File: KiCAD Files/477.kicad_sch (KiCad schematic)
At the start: 28 parts, among them IC1 W25N01GVSFIG, IC2 W25N01GVSFIG, IC3 W25N01GVSFIG, IC4 W25N01GVSFIG, IC6 USBLC6-2SC6, J1 BM06B-SRSS-TBT_LF__SN_, J2 6364372-2, J5 BM07B-SRSS-TB_LF__SN_, J6 BM09B-SRSS-TB_LF__SN_

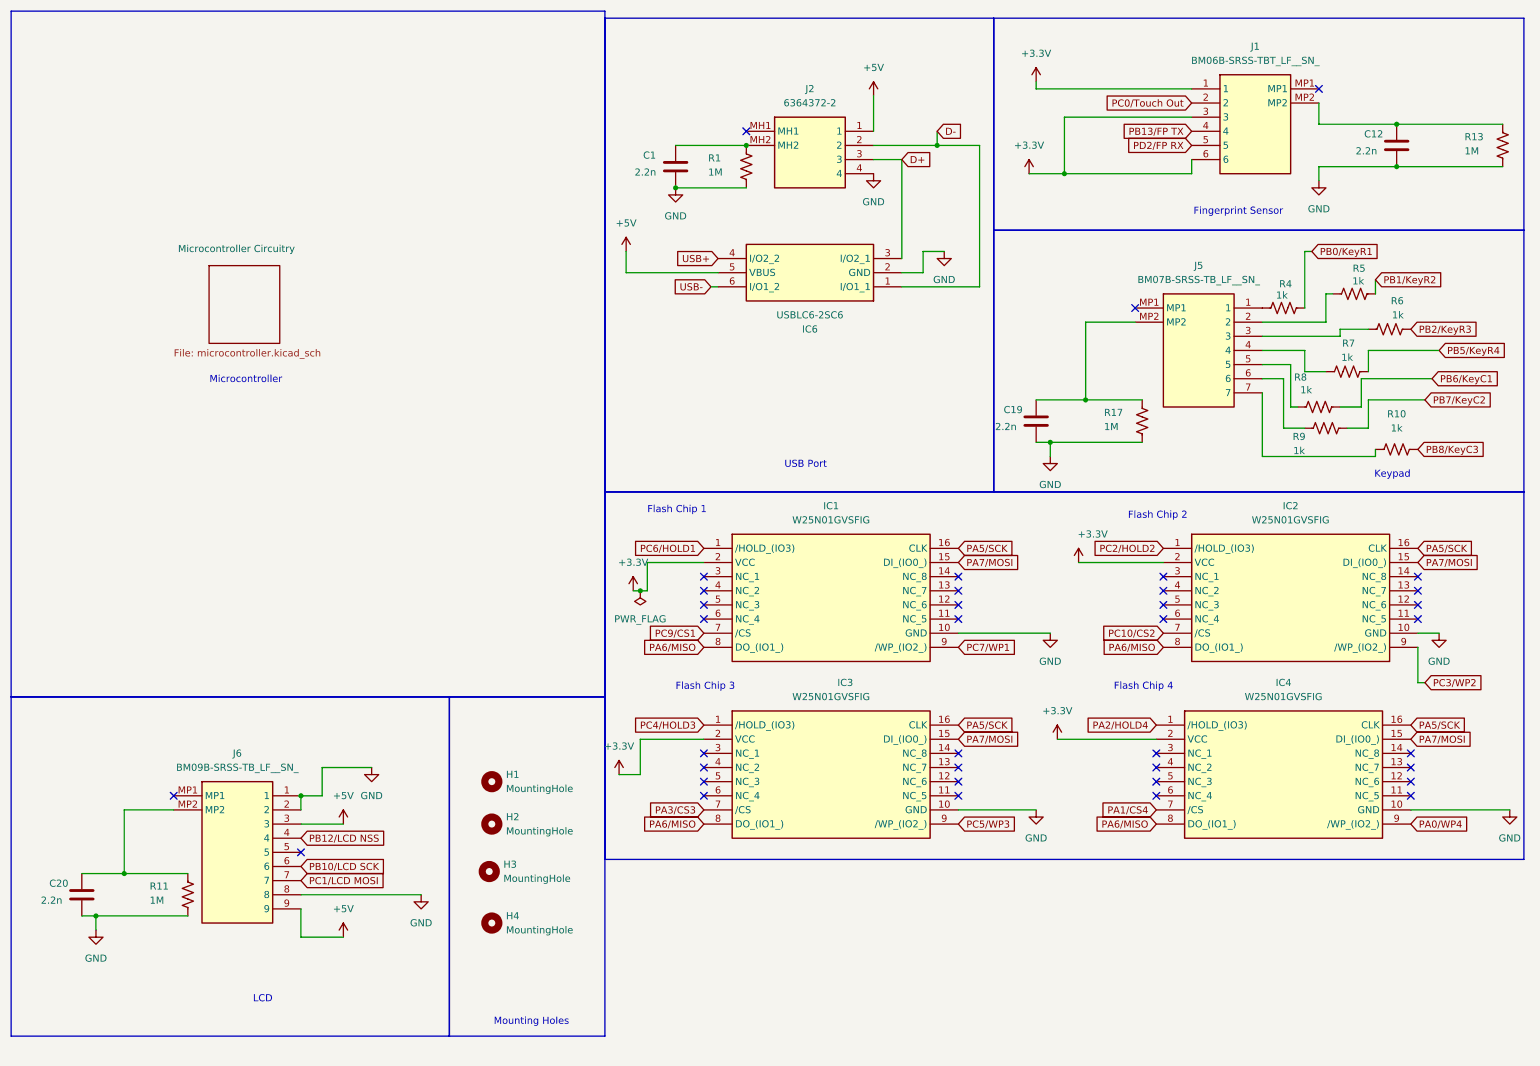
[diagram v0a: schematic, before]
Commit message: Finalized Signal Routing
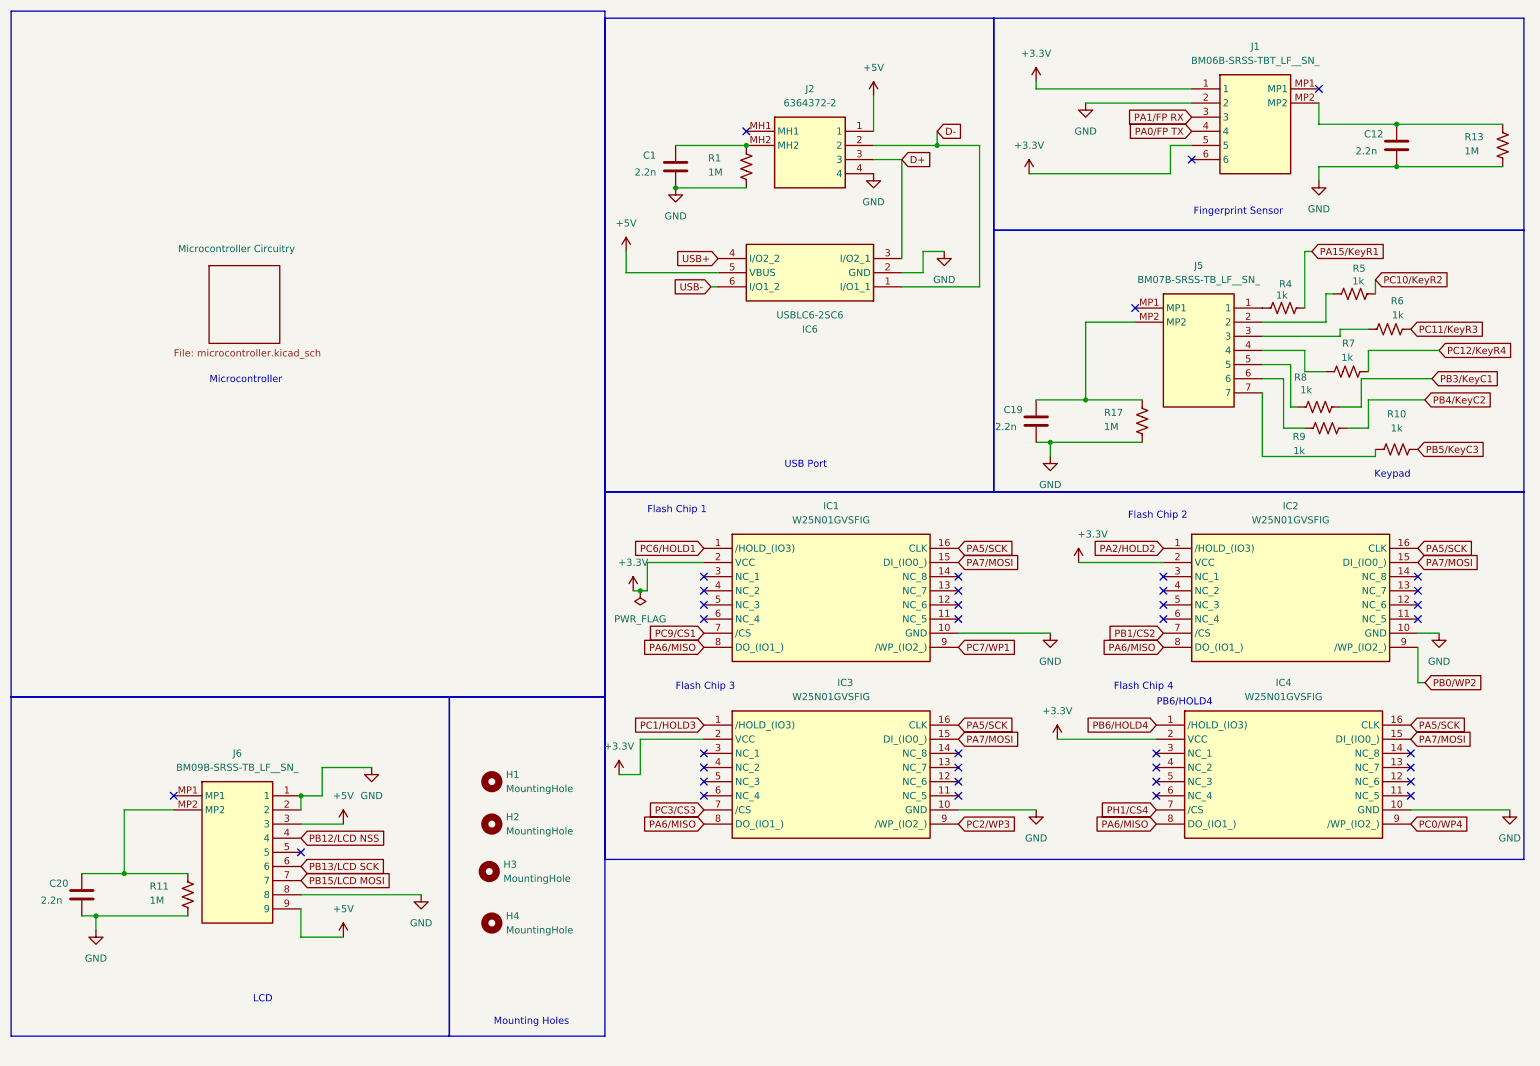
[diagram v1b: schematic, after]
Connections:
- net PC0/Touch Out is gone; now on net GND: J1.2
- net PD2/FP RX is gone; now on net +3.3V: J1.5
- net +3.3V: no longer J1.3, J1.6
- net PA0/WP4 renamed PC0/WP4
- net PA1/CS4 renamed PH1/CS4
- net PA2/HOLD4 renamed PB6/HOLD4
- net PA3/CS3 renamed PC3/CS3
- net PB0/KeyR1 renamed PA15/KeyR1
- net PB10/LCD SCK renamed PB13/LCD SCK
- net PB13/FP TX renamed PA0/FP TX
- net PB1/KeyR2 renamed PC10/KeyR2
- net PB2/KeyR3 renamed PC11/KeyR3
- net PB5/KeyR4 renamed PC12/KeyR4
- net PB6/KeyC1 renamed PB3/KeyC1
- net PB7/KeyC2 renamed PB4/KeyC2
- net PB8/KeyC3 renamed PB5/KeyC3
- net PC10/CS2 renamed PB1/CS2
- net PC1/LCD MOSI renamed PB15/LCD MOSI
- net PC2/HOLD2 renamed PA2/HOLD2
- net PC3/WP2 renamed PB0/WP2
- net PC4/HOLD3 renamed PC1/HOLD3
- net PC5/WP3 renamed PC2/WP3
- new net PA1/FP RX: J1.3
- no-connect marks 37 -> 38
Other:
- note added: "PB6/HOLD4"

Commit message: updated files with 3d models
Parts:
- removed H1, H2, H3, H4: MountingHole, MountingHole:MountingHole_3.2mm_M3_DIN965, symbol Mechanical:MountingHole
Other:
- note added: "Fingerprint Sensor Connector"
- note added: "Keypad Connector"
- note added: "LCD Connector"
- note added: "USB Port with ESD protection"
- note removed: "Fingerprint Sensor"
- note removed: "Keypad"
- note removed: "LCD"
- note removed: "Mounting Holes"
- note removed: "USB Port"

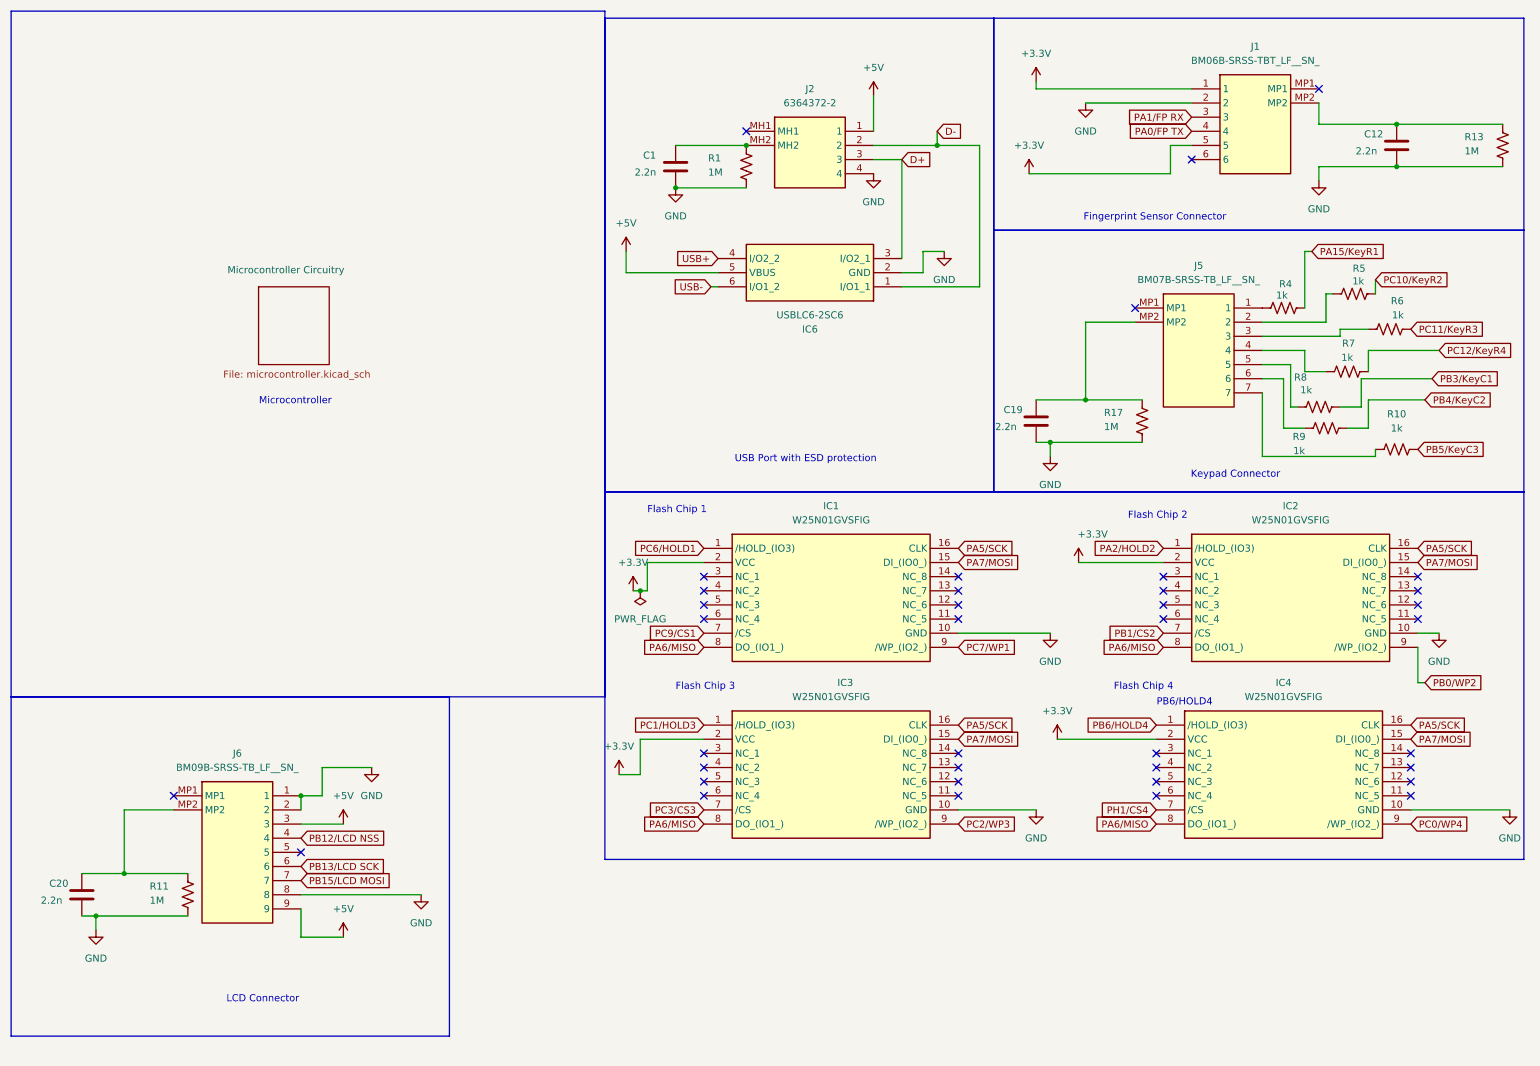
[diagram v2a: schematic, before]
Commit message: added esd changes to schematic and pcb, mainly for J1 and J5, no DRC run
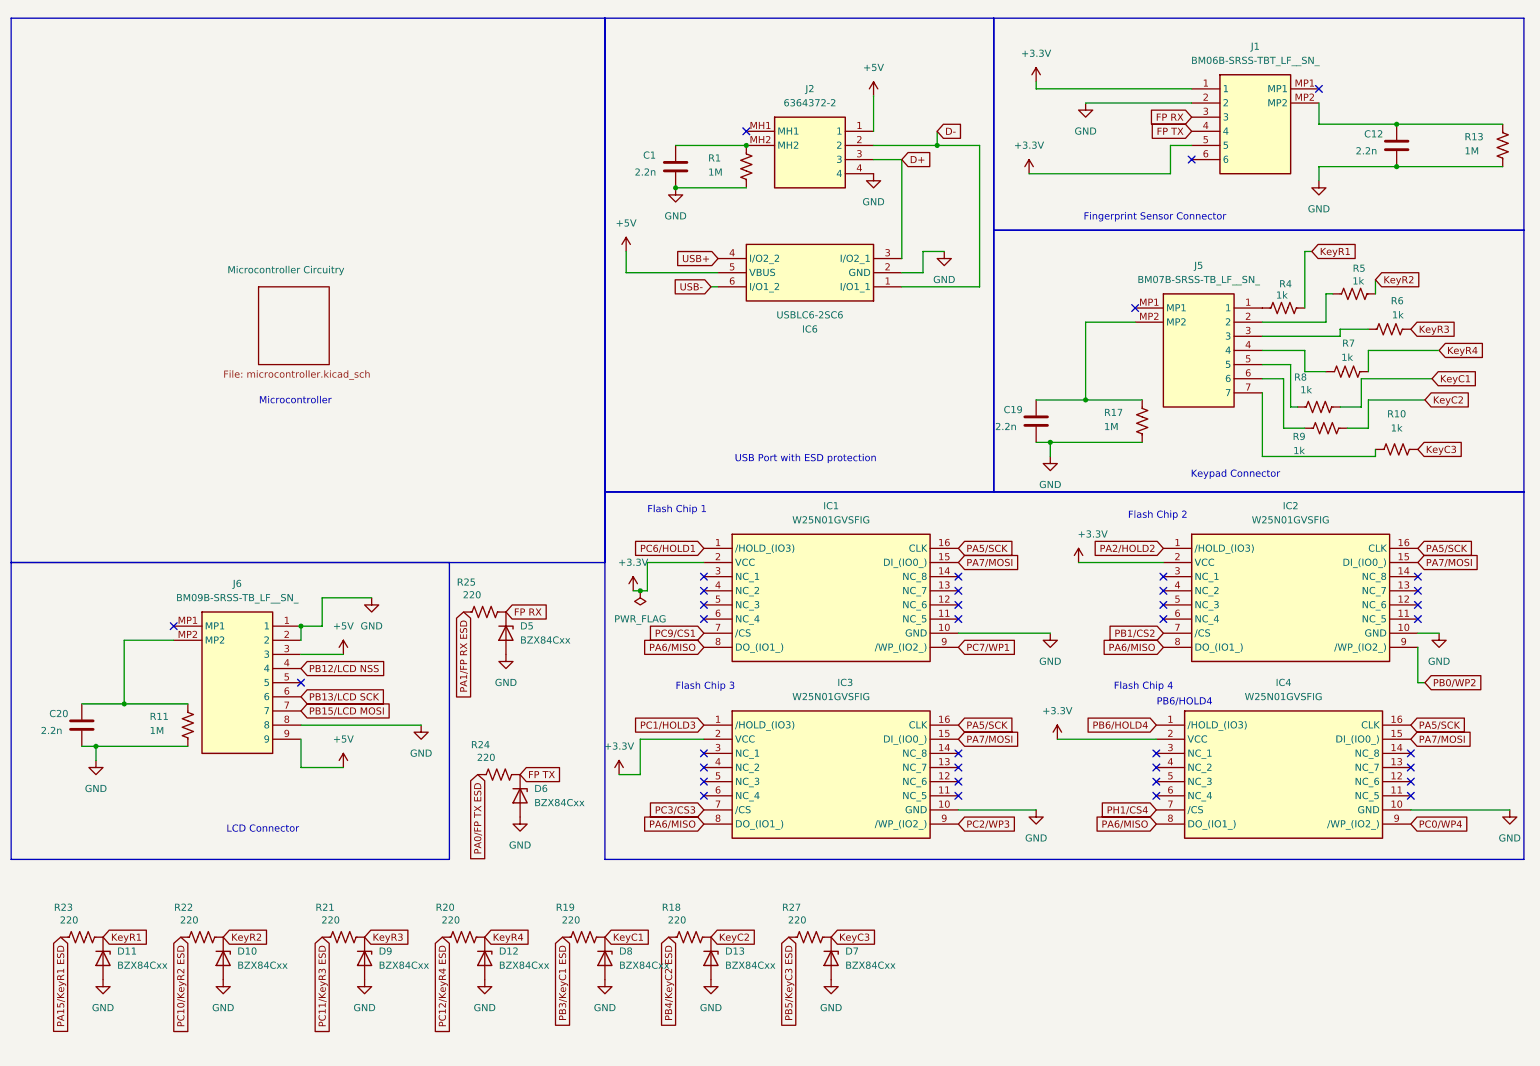
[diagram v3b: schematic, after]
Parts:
- added D10, D11, D12, D13, D5, D6, D7, D8, D9: BZX84Cxx, Package_TO_SOT_SMD:SOT-23, symbol Diode:BZX84Cxx
- added R18, R19, R20, R21, R22, R23, R24, R25, R27: 220, Resistor_SMD:R_0805_2012Metric_Pad1.20x1.40mm_HandSolder, symbol CustomSymbols:R_US
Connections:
- net GND: now also D10.1 (A), D11.1 (A), D12.1 (A), D13.1 (A), D5.1 (A), D6.1 (A), D7.1 (A), D8.1 (A), D9.1 (A)
- net PA0/FP TX renamed FP TX
- net FP TX: now also D6.3 (K), R24.1
- net PA15/KeyR1 renamed KeyR1
- net KeyR1: now also D11.3 (K), R23.1
- net PA1/FP RX renamed FP RX
- net FP RX: now also D5.3 (K), R25.1
- net PB3/KeyC1 renamed KeyC1
- net KeyC1: now also D8.3 (K), R19.1
- net PB4/KeyC2 renamed KeyC2
- net KeyC2: now also D13.3 (K), R18.1
- net PB5/KeyC3 renamed KeyC3
- net KeyC3: now also D7.3 (K), R27.1
- net PC10/KeyR2 renamed KeyR2
- net KeyR2: now also D10.3 (K), R22.1
- net PC11/KeyR3 renamed KeyR3
- net KeyR3: now also D9.3 (K), R21.1
- net PC12/KeyR4 renamed KeyR4
- net KeyR4: now also D12.3 (K), R20.1
- new net PA0/FP TX ESD: R24.2
- new net PA15/KeyR1 ESD: R23.2
- new net PA1/FP RX ESD: R25.2
- new net PB3/KeyC1 ESD: R19.2
- new net PB4/KeyC2 ESD: R18.2
- new net PB5/KeyC3 ESD: R27.2
- new net PC10/KeyR2 ESD: R22.2
- new net PC11/KeyR3 ESD: R21.2
- new net PC12/KeyR4 ESD: R20.2
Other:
- moved on the sheet: C20, J6, R11

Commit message: rerouted keypad
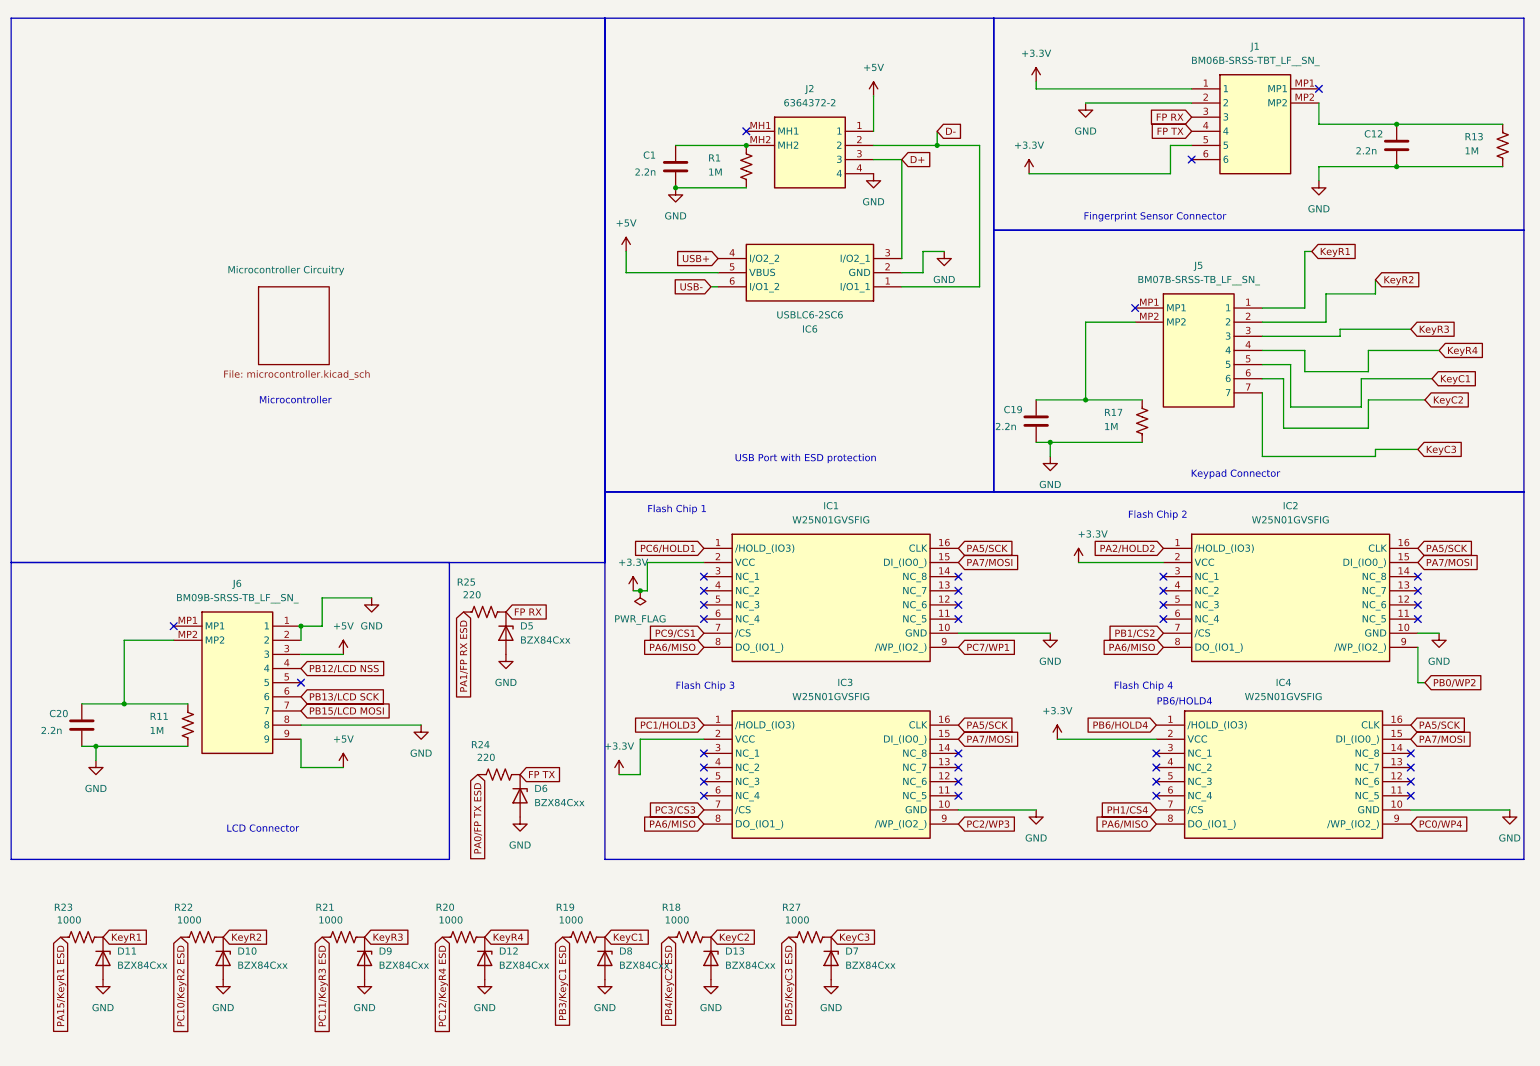
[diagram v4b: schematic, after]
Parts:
- removed R10, R4, R5, R6, R7, R8, R9: 1k, Resistor_SMD:R_0805_2012Metric_Pad1.20x1.40mm_HandSolder, symbol CustomSymbols:R_US
- R18, R19, R20, R21, R22, R23, R27: value 220 -> 1000
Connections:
- net KeyC1: now also J5.5
- net KeyC2: now also J5.6
- net KeyC3: now also J5.7
- net KeyR1: now also J5.1
- net KeyR2: now also J5.2
- net KeyR3: now also J5.3
- net KeyR4: now also J5.4
